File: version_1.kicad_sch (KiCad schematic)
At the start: 32 parts, among them U1 Pico, U10 74HCT595D, U12 C967633, U18 SM04B-SRSS-TB_(LF)(SN), U3 L7805CD2T-TR

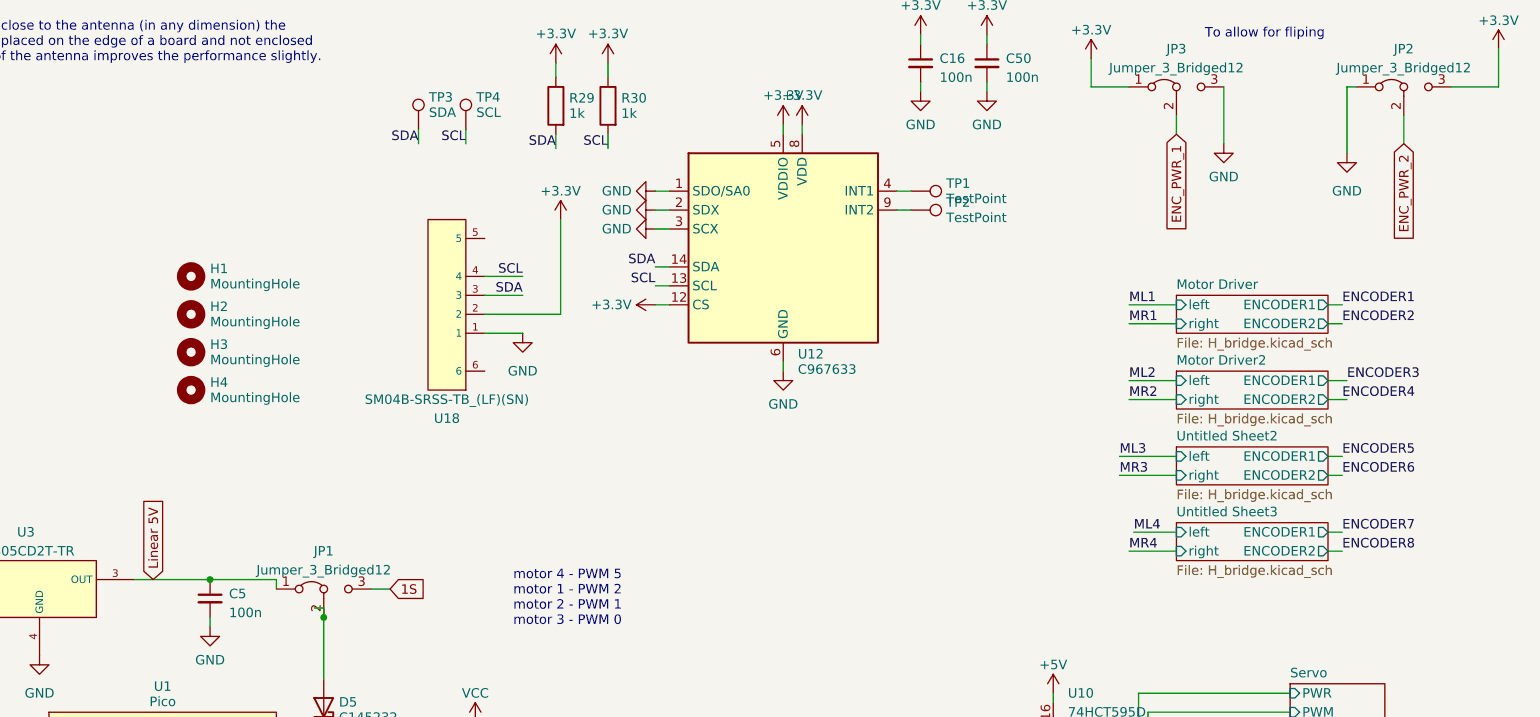
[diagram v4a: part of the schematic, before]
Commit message: encoder power fliping
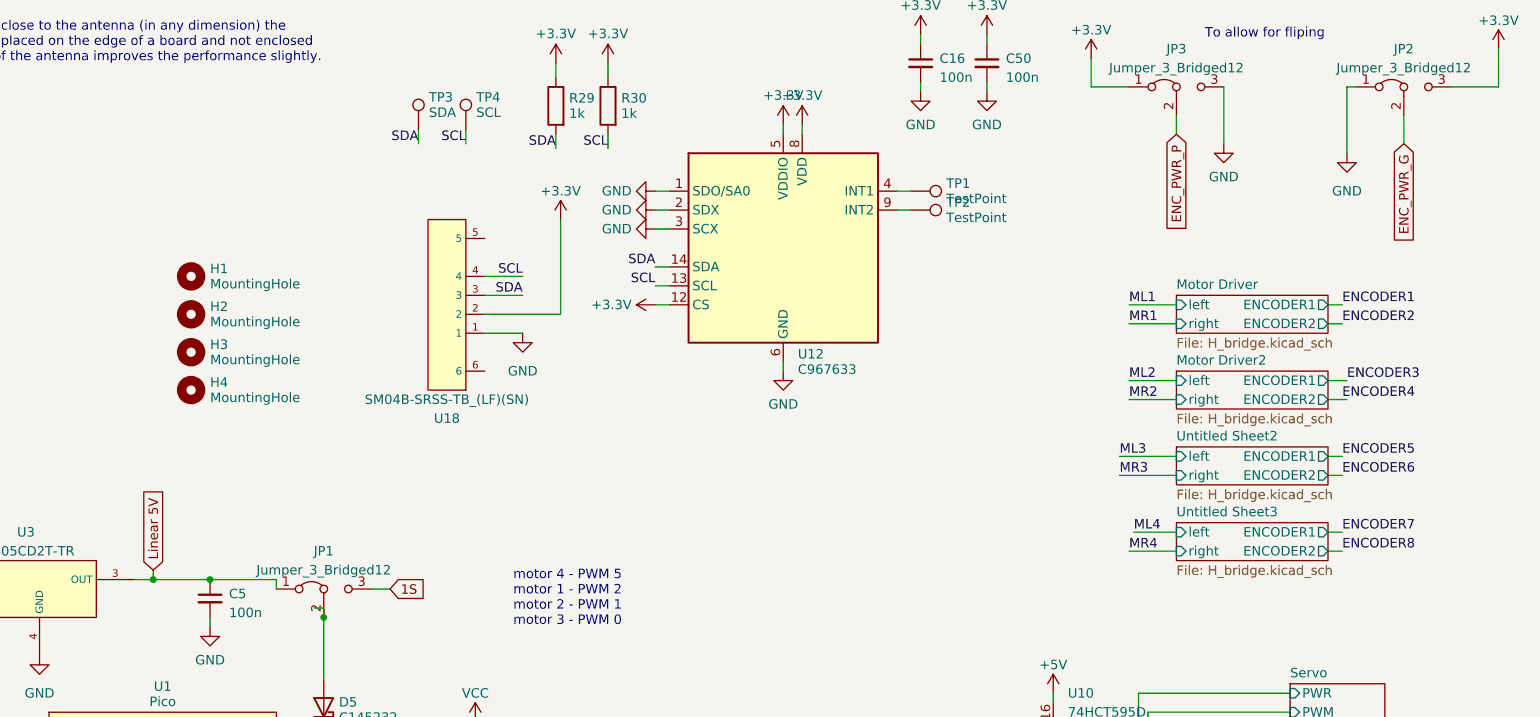
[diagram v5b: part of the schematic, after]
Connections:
- net ENC_PWR_1 renamed ENC_PWR_P
- net ENC_PWR_2 renamed ENC_PWR_G
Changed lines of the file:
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@@
   (junction (at 144.78 127) (diameter 0) (color 0 0 0 0)
+  )
+  (junction (at 101.6 91.44) (diameter 0) (color 0 0 0 0)
   )
   (junction (at 71.12 91.44) (diameter 0) (color 0 0 0 0)
@@
     (stroke (width 0) (type default))
   )
+  (wire (pts (xy 101.6 91.44) (xy 109.22 91.44))
+    (stroke (width 0) (type default))
+  )
   (wire (pts (xy 281.94 25.4) (xy 281.94 20.32))
     (stroke (width 0) (type default))
@@
     (stroke (width 0) (type default))
   )
+  (wire (pts (xy 101.6 90.17) (xy 101.6 91.44))
+    (stroke (width 0) (type default))
+  )
   (wire (pts (xy 70.485 119.38) (xy 76.835 119.38))
     (stroke (width 0) (type default))
@@
     (stroke (width 0) (type default))
   )
-  (wire (pts (xy 99.06 91.44) (xy 109.22 91.44))
+  (wire (pts (xy 99.06 91.44) (xy 101.6 91.44))
     (stroke (width 0) (type default))
   )
@@
     (effects (font (size 1.27 1.27)) (justify right bottom))
   )
-  (global_label "ENC_PWR_1" (shape input) (at 238.76 31.75 270) (fields_autoplaced)
+  (global_label "ENC_PWR_P" (shape input) (at 238.76 31.75 270) (fields_autoplaced)
     (effects (font (size 1.27 1.27)) (justify right))
-    (property "Intersheetrefs" "${INTERSHEET_REFS}" (at 238.76 45.5414 90)
+    (property "Intersheetrefs" "${INTERSHEET_REFS}" (at 238.76 45.6019 90)
       (effects (font (size 1.27 1.27)) (justify right) hide)
     )
   )
-  (global_label "Linear 5V" (shape input) (at 101.6 91.44 90) (fields_autoplaced)
+  (global_label "Linear 5V" (shape input) (at 101.6 90.17 90) (fields_autoplaced)
     (effects (font (size 1.27 1.27)) (justify left))
-    (property "Intersheetrefs" "${INTERSHEET_REFS}" (at 101.6 79.4628 90)
+    (property "Intersheetrefs" "${INTERSHEET_REFS}" (at 101.6 78.1928 90)
       (effects (font (size 1.27 1.27)) (justify left) hide)
     )
@@
     )
   )
-  (global_label "ENC_PWR_2" (shape input) (at 269.24 33.02 270) (fields_autoplaced)
+  (global_label "ENC_PWR_G" (shape input) (at 269.24 33.02 270) (fields_autoplaced)
     (effects (font (size 1.27 1.27)) (justify right))
-    (property "Intersheetrefs" "${INTERSHEET_REFS}" (at 269.24 46.8114 90)
+    (property "Intersheetrefs" "${INTERSHEET_REFS}" (at 269.24 46.8719 90)
       (effects (font (size 1.27 1.27)) (justify right) hide)
     )

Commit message: big layout changes
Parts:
- removed TP1, TP2: TestPoint, TestPoint:TestPoint_Pad_D2.0mm, symbol Connector:TestPoint
- removed TP3: SDA, TestPoint:TestPoint_Pad_D2.0mm, symbol Connector:TestPoint
- removed TP4: SCL, TestPoint:TestPoint_Pad_D2.0mm, symbol Connector:TestPoint
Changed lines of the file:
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@@
-    (stroke (width 0) (type default))
-  )
-  (wire (pts (xy 143.51 31.115) (xy 143.51 33.02))
     (stroke (width 0) (type default))
   )
@@
   )
   (wire (pts (xy 188.595 30.48) (xy 188.595 31.75))
-    (stroke (width 0) (type default))
-  )
-  (wire (pts (xy 137.16 31.115) (xy 137.16 33.02))
     (stroke (width 0) (type default))
   )
@@
     (effects (font (size 1.27 1.27)) (justify left bottom))
   )
-  (label "SDA" (at 137.16 33.02 180) (fields_autoplaced)
-    (effects (font (size 1.27 1.27)) (justify right bottom))
-  )
   (label "ENCODER8" (at 78.105 139.7 180) (fields_autoplaced)
     (effects (font (size 1.27 1.27)) (justify right bottom))
@@
   (label "ML2" (at 126.365 149.86 0) (fields_autoplaced)
     (effects (font (size 1.27 1.27)) (justify left bottom))
-  )
-  (label "SCL" (at 143.51 33.02 180) (fields_autoplaced)
-    (effects (font (size 1.27 1.27)) (justify right bottom))
   )
   (label "SDA" (at 83.185 119.38 180) (fields_autoplaced)
@@
     (property "Intersheetrefs" "${INTERSHEET_REFS}" (at 269.24 46.8719 90)
       (effects (font (size 1.27 1.27)) (justify right) hide)
-    )
-  )
-  (symbol (lib_id "Connector:TestPoint") (at 143.51 31.115 0) (unit 1)
-    (in_bom yes) (on_board yes) (dnp no) (fields_autoplaced)
-    (property "Reference" "TP4" (at 144.907 26.789 0)
-      (effects (font (size 1.27 1.27)) (justify left))
-    )
-    (property "Value" "SCL" (at 144.907 28.837 0)
-      (effects (font (size 1.27 1.27)) (justify left))
-    )
-    (property "Footprint" "TestPoint:TestPoint_Pad_D2.0mm" (at 148.59 31.115 0)
-      (effects (font (size 1.27 1.27)) hide)
-    )
-    (property "Datasheet" "~" (at 148.59 31.115 0)
-      (effects (font (size 1.27 1.27)) hide)
-    )
-    (pin "1")
-    (instances
-      (project "version_1"
-        (path "/23ba0750-4a55-4d50-828b-749cc0fbb8c8"
-          (reference "TP4") (unit 1)
-        )
-      )
     )
   )
@@
     )
   )
-  (symbol (lib_id "Connector:TestPoint") (at 203.2 41.91 270) (unit 1)
-    (in_bom yes) (on_board yes) (dnp no) (fields_autoplaced)
-    (property "Reference" "TP2" (at 207.899 40.886 90)
-      (effects (font (size 1.27 1.27)) (justify left))
-    )
-    (property "Value" "TestPoint" (at 207.899 42.934 90)
-      (effects (font (size 1.27 1.27)) (justify left))
-    )
-    (property "Footprint" "TestPoint:TestPoint_Pad_D2.0mm" (at 203.2 46.99 0)
-      (effects (font (size 1.27 1.27)) hide)
-    )
-    (property "Datasheet" "~" (at 203.2 46.99 0)
-      (effects (font (size 1.27 1.27)) hide)
-    )
-    (pin "1")
-    (instances
-      (project "version_1"
-        (path "/23ba0750-4a55-4d50-828b-749cc0fbb8c8"
-          (reference "TP2") (unit 1)
-        )
-      )
-    )
-  )
   (symbol (lib_id "power:GND") (at 109.22 97.79 0) (unit 1)
     (in_bom yes) (on_board yes) (dnp no) (fields_autoplaced)
@@
         (path "/23ba0750-4a55-4d50-828b-749cc0fbb8c8"
           (reference "#PWR014") (unit 1)
-        )
-      )
-    )
-  )
-  (symbol (lib_id "Connector:TestPoint") (at 137.16 31.115 0) (unit 1)
-    (in_bom yes) (on_board yes) (dnp no) (fields_autoplaced)
-    (property "Reference" "TP3" (at 138.557 26.789 0)
-      (effects (font (size 1.27 1.27)) (justify left))
-    )
-    (property "Value" "SDA" (at 138.557 28.837 0)
-      (effects (font (size 1.27 1.27)) (justify left))
-    )
-    (property "Footprint" "TestPoint:TestPoint_Pad_D2.0mm" (at 142.24 31.115 0)
-      (effects (font (size 1.27 1.27)) hide)
-    )
-    (property "Datasheet" "~" (at 142.24 31.115 0)
-      (effects (font (size 1.27 1.27)) hide)
-    )
-    (pin "1")
-    (instances
-      (project "version_1"
-        (path "/23ba0750-4a55-4d50-828b-749cc0fbb8c8"
-          (reference "TP3") (unit 1)
         )
       )
@@
         )
       )
-    )
-  )
-  (symbol (lib_id "Connector:TestPoint") (at 203.2 39.37 270) (unit 1)
-    (in_bom yes) (on_board yes) (dnp no) (fields_autoplaced)
-    (property "Reference" "TP1" (at 207.899 38.346 90)
-      (effects (font (size 1.27 1.27)) (justify left))
-    )
-    (property "Value" "TestPoint" (at 207.899 40.394 90)
-      (effects (font (size 1.27 1.27)) (justify left))
-    )
-    (property "Footprint" "TestPoint:TestPoint_Pad_D2.0mm" (at 203.2 44.45 0)
-      (effects (font (size 1.27 1.27)) hide)
-    )
-    (property "Datasheet" "~" (at 203.2 44.45 0)
-      (effects (font (size 1.27 1.27)) hide)
-    )
-    (pin "1")
-    (instances
-      (project "version_1"
-        (path "/23ba0750-4a55-4d50-828b-749cc0fbb8c8"
-          (reference "TP1") (unit 1)
-        )
-      )

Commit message: tetris
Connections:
- net ENCODER1: now also U1.19 (GPIO14); no longer U1.14 (GPIO10)
- net ENCODER2: now also U1.20 (GPIO15); no longer U1.15 (GPIO11)
- net ENCODER5: now also U1.14 (GPIO10); no longer U1.19 (GPIO14)
- net ENCODER6: now also U1.15 (GPIO11); no longer U1.20 (GPIO15)
- net ML1: now also U1.21 (GPIO16); no longer U1.27 (GPIO21)
- net ML2: now also U1.24 (GPIO18); no longer U1.25 (GPIO19)
- net ML3: now also U1.26 (GPIO20); no longer U1.22 (GPIO17)
- net ML4: now also U1.31 (GPIO26_ADC0); no longer U1.32 (GPIO27_ADC1)
- net MR1: now also U1.22 (GPIO17); no longer U1.26 (GPIO20)
- net MR2: now also U1.25 (GPIO19); no longer U1.24 (GPIO18)
- net MR3: now also U1.27 (GPIO21); no longer U1.21 (GPIO16)
- net MR4: now also U1.32 (GPIO27_ADC1); no longer U1.31 (GPIO26_ADC0)
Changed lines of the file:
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@@
+    (stroke (width 0) (type default))
+  )
+  (wire (pts (xy 120.65 149.86) (xy 127 149.86))
     (stroke (width 0) (type default))
   )
@@
     (stroke (width 0) (type default))
   )
-  (wire (pts (xy 126.365 147.32) (xy 120.65 147.32))
-    (stroke (width 0) (type default))
-  )
-  (wire (pts (xy 126.365 144.78) (xy 120.65 144.78))
+  (wire (pts (xy 120.65 147.32) (xy 127 147.32))
+    (stroke (width 0) (type default))
+  )
+  (wire (pts (xy 120.65 144.78) (xy 127 144.78))
     (stroke (width 0) (type default))
   )
@@
     (stroke (width 0) (type default))
   )
-  (wire (pts (xy 78.105 157.48) (xy 85.09 157.48))
+  (wire (pts (xy 77.47 157.48) (xy 85.09 157.48))
     (stroke (width 0) (type default))
   )
@@
     (stroke (width 0) (type default))
   )
-  (wire (pts (xy 120.65 157.48) (xy 126.365 157.48))
+  (wire (pts (xy 120.65 157.48) (xy 127 157.48))
     (stroke (width 0) (type default))
   )
@@
     (stroke (width 0) (type default))
   )
-  (wire (pts (xy 120.65 160.02) (xy 126.365 160.02))
+  (wire (pts (xy 120.65 160.02) (xy 127 160.02))
     (stroke (width 0) (type default))
   )
@@
     (stroke (width 0) (type default))
   )
-  (wire (pts (xy 68.58 137.16) (xy 85.09 137.16))
+  (wire (pts (xy 77.47 137.16) (xy 85.09 137.16))
     (stroke (width 0) (type default))
   )
@@
     (stroke (width 0) (type default))
   )
-  (wire (pts (xy 78.105 147.32) (xy 85.09 147.32))
-    (stroke (width 0) (type default))
-  )
   (wire (pts (xy 41.91 119.38) (xy 43.815 119.38))
     (stroke (width 0) (type default))
@@
     (stroke (width 0) (type default))
   )
+  (wire (pts (xy 76.2 147.32) (xy 85.09 147.32))
+    (stroke (width 0) (type default))
+  )
   (wire (pts (xy 158.75 128.905) (xy 158.75 127))
     (stroke (width 0) (type default))
@@
     (stroke (width 0) (type default))
   )
+  (wire (pts (xy 77.47 160.02) (xy 85.09 160.02))
+    (stroke (width 0) (type default))
+  )
   (wire (pts (xy 168.91 41.91) (xy 170.815 41.91))
     (stroke (width 0) (type default))
@@
     (stroke (width 0) (type default))
   )
-  (wire (pts (xy 126.365 132.08) (xy 120.65 132.08))
+  (wire (pts (xy 120.65 132.08) (xy 127 132.08))
     (stroke (width 0) (type default))
   )
@@
     (stroke (width 0) (type default))
   )
-  (wire (pts (xy 126.365 134.62) (xy 120.65 134.62))
+  (wire (pts (xy 120.65 152.4) (xy 127 152.4))
+    (stroke (width 0) (type default))
+  )
+  (wire (pts (xy 120.65 134.62) (xy 127 134.62))
     (stroke (width 0) (type default))
   )
@@
     (stroke (width 0) (type default))
   )
-  (wire (pts (xy 78.105 160.02) (xy 85.09 160.02))
-    (stroke (width 0) (type default))
-  )
   (wire (pts (xy 200.025 113.03) (xy 212.09 113.03))
     (stroke (width 0) (type default))
@@
     (stroke (width 0) (type default))
   )
-  (wire (pts (xy 78.105 144.78) (xy 85.09 144.78))
+  (wire (pts (xy 76.2 144.78) (xy 85.09 144.78))
     (stroke (width 0) (type default))
   )
@@
     (stroke (width 0) (type default))
   )
-  (wire (pts (xy 120.65 152.4) (xy 126.365 152.4))
-    (stroke (width 0) (type default))
-  )
   (wire (pts (xy 120.65 139.7) (xy 140.97 139.7))
     (stroke (width 0) (type default))
@@
   )
   (wire (pts (xy 70.485 109.22) (xy 76.835 109.22))
-    (stroke (width 0) (type default))
-  )
-  (wire (pts (xy 120.65 149.86) (xy 126.365 149.86))
     (stroke (width 0) (type default))
   )
@@
     (effects (font (size 1.27 1.27)) (justify left bottom))
   )
-  (label "ENCODER7" (at 68.58 137.16 0) (fields_autoplaced)
-    (effects (font (size 1.27 1.27)) (justify left bottom))
+  (label "ENCODER7" (at 77.47 137.16 180) (fields_autoplaced)
+    (effects (font (size 1.27 1.27)) (justify right bottom))
   )
   (label "SCL" (at 151.13 50.8 180) (fields_autoplaced)
     (effects (font (size 1.27 1.27)) (justify right bottom))
   )
-  (label "MR4" (at 126.365 134.62 0) (fields_autoplaced)
+  (label "MR4" (at 127 132.08 0) (fields_autoplaced)
+    (effects (font (size 1.27 1.27)) (justify left bottom))
+  )
+  (label "MR3" (at 127 144.78 0) (fields_autoplaced)
     (effects (font (size 1.27 1.27)) (justify left bottom))
   )
@@
     (effects (font (size 1.27 1.27)) (justify left bottom))
   )
-  (label "MR3" (at 126.365 160.02 0) (fields_autoplaced)
-    (effects (font (size 1.27 1.27)) (justify left bottom))
-  )
-  (label "ENCODER2" (at 78.105 147.32 180) (fields_autoplaced)
+  (label "ENCODER6" (at 76.2 147.32 180) (fields_autoplaced)
     (effects (font (size 1.27 1.27)) (justify right bottom))
   )
@@
     (effects (font (size 1.27 1.27)) (justify left bottom))
   )
-  (label "MR2" (at 126.365 152.4 0) (fields_autoplaced)
+  (label "MR2" (at 127 149.86 0) (fields_autoplaced)
     (effects (font (size 1.27 1.27)) (justify left bottom))
   )
@@
     (effects (font (size 1.27 1.27)) (justify left bottom))
   )
+  (label "ENCODER1" (at 77.47 157.48 180) (fields_autoplaced)
+    (effects (font (size 1.27 1.27)) (justify right bottom))
+  )
   (label "ENCODER3" (at 78.105 149.86 180) (fields_autoplaced)
     (effects (font (size 1.27 1.27)) (justify right bottom))
   )
+  (label "ML3" (at 127 147.32 0) (fields_autoplaced)
+    (effects (font (size 1.27 1.27)) (justify left bottom))
+  )
   (label "PWM_CLK" (at 200.025 118.11 0) (fields_autoplaced)
     (effects (font (size 1.27 1.27)) (justify left bottom))
@@
     (effects (font (size 1.27 1.27)) (justify left bottom))
   )
-  (label "MR1" (at 126.365 147.32 0) (fields_autoplaced)
+  (label "ML1" (at 127 160.02 0) (fields_autoplaced)
     (effects (font (size 1.27 1.27)) (justify left bottom))
   )
@@
     (effects (font (size 1.27 1.27)) (justify left bottom))
   )
-  (label "ML3" (at 126.365 157.48 0) (fields_autoplaced)
-    (effects (font (size 1.27 1.27)) (justify left bottom))
-  )
   (label "ML1" (at 232.41 54.61 0) (fields_autoplaced)
     (effects (font (size 1.27 1.27)) (justify left bottom))
   )
-  (label "ML1" (at 126.365 144.78 0) (fields_autoplaced)
-    (effects (font (size 1.27 1.27)) (justify left bottom))
+  (label "ENCODER2" (at 77.47 160.02 180) (fields_autoplaced)
+    (effects (font (size 1.27 1.27)) (justify right bottom))
   )
   (label "PWM_CLK" (at 74.295 132.08 0) (fields_autoplaced)
@@
     (effects (font (size 1.27 1.27)) (justify right bottom))
   )
+  (label "ENCODER5" (at 76.2 144.78 180) (fields_autoplaced)
+    (effects (font (size 1.27 1.27)) (justify right bottom))
+  )
   (label "PWM_DATA" (at 200.025 113.03 0) (fields_autoplaced)
     (effects (font (size 1.27 1.27)) (justify left bottom))
   )
-  (label "ENCODER6" (at 78.105 160.02 180) (fields_autoplaced)
-    (effects (font (size 1.27 1.27)) (justify right bottom))
-  )
-  (label "ML4" (at 126.365 132.08 0) (fields_autoplaced)
+  (label "ML4" (at 127 134.62 0) (fields_autoplaced)
     (effects (font (size 1.27 1.27)) (justify left bottom))
   )
@@
     (effects (font (size 1.27 1.27)) (justify left bottom))
   )
-  (label "ENCODER1" (at 78.105 144.78 180) (fields_autoplaced)
-    (effects (font (size 1.27 1.27)) (justify right bottom))
-  )
   (label "MR3" (at 231.14 77.47 0) (fields_autoplaced)
     (effects (font (size 1.27 1.27)) (justify left bottom))
@@
     (effects (font (size 1.27 1.27)) (justify left bottom))
   )
-  (label "ENCODER5" (at 78.105 157.48 180) (fields_autoplaced)
-    (effects (font (size 1.27 1.27)) (justify right bottom))
+  (label "MR1" (at 127 157.48 0) (fields_autoplaced)
+    (effects (font (size 1.27 1.27)) (justify left bottom))
   )
   (label "ML2" (at 232.41 64.77 0) (fields_autoplaced)
@@
     (effects (font (size 1.27 1.27)) (justify left bottom))
   )
-  (label "ML2" (at 126.365 149.86 0) (fields_autoplaced)
-    (effects (font (size 1.27 1.27)) (justify left bottom))
-  )
+  (label "ML2" (at 127 152.4 0) (fields_autoplaced)
+    (effects (font (size 1.27 1.27)) (justify left bottom))
+  )
